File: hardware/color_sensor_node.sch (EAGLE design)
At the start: 20 parts, among them Q1 20V/4.2A/52mΩ/1.4W, U1 ISL29125, U2 3.3V, U3 WS2811

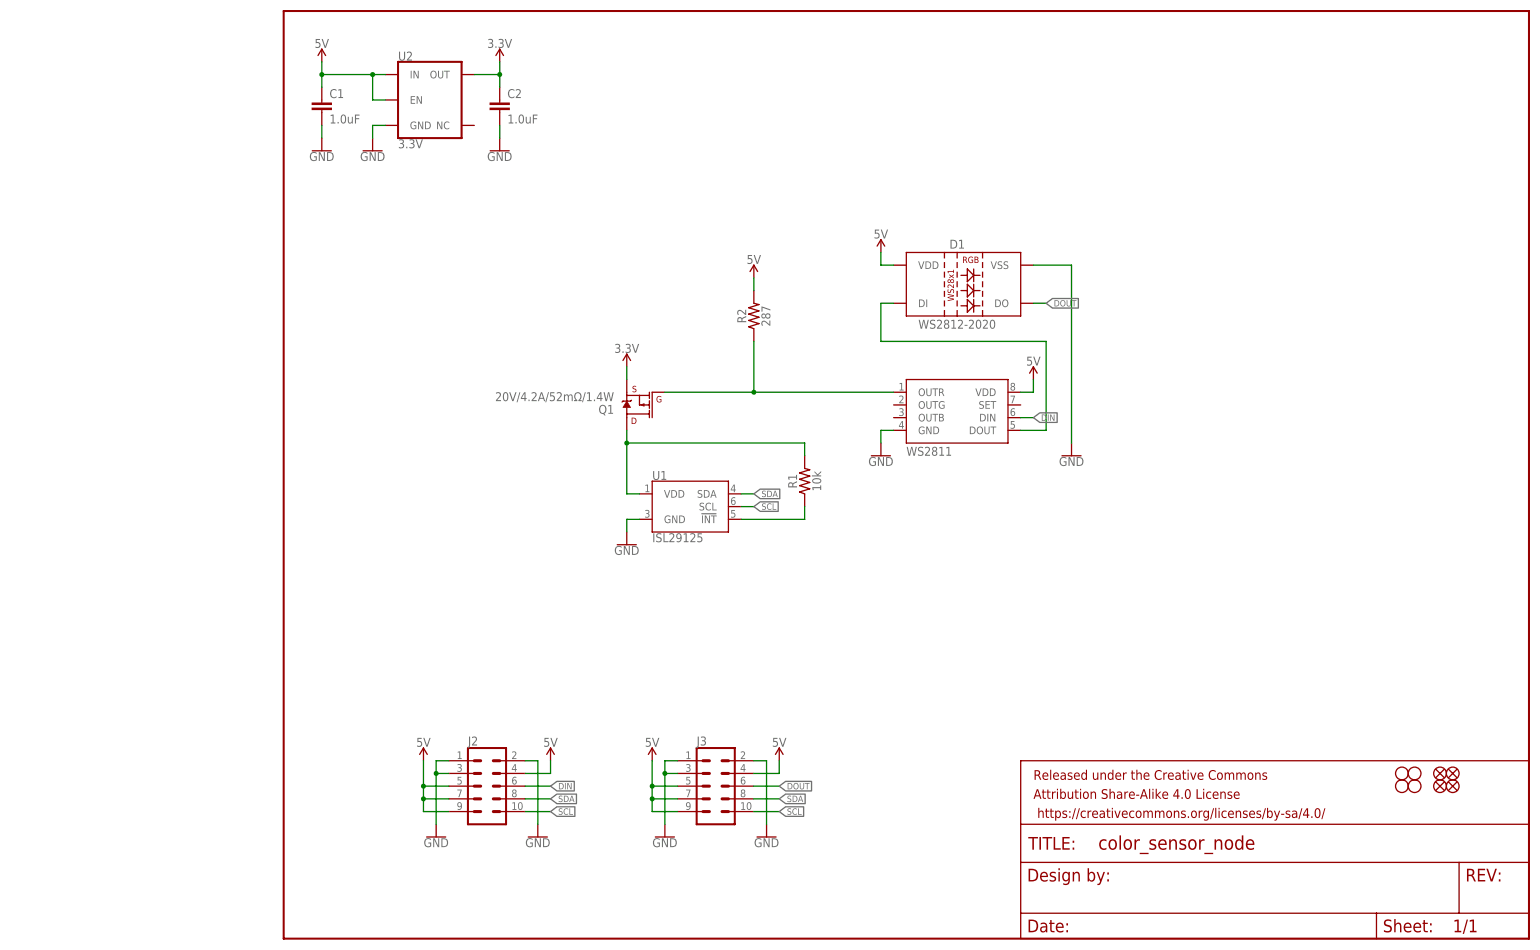
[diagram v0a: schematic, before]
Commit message: update packages, add rc filter to sensor vdd, move to smd connectors
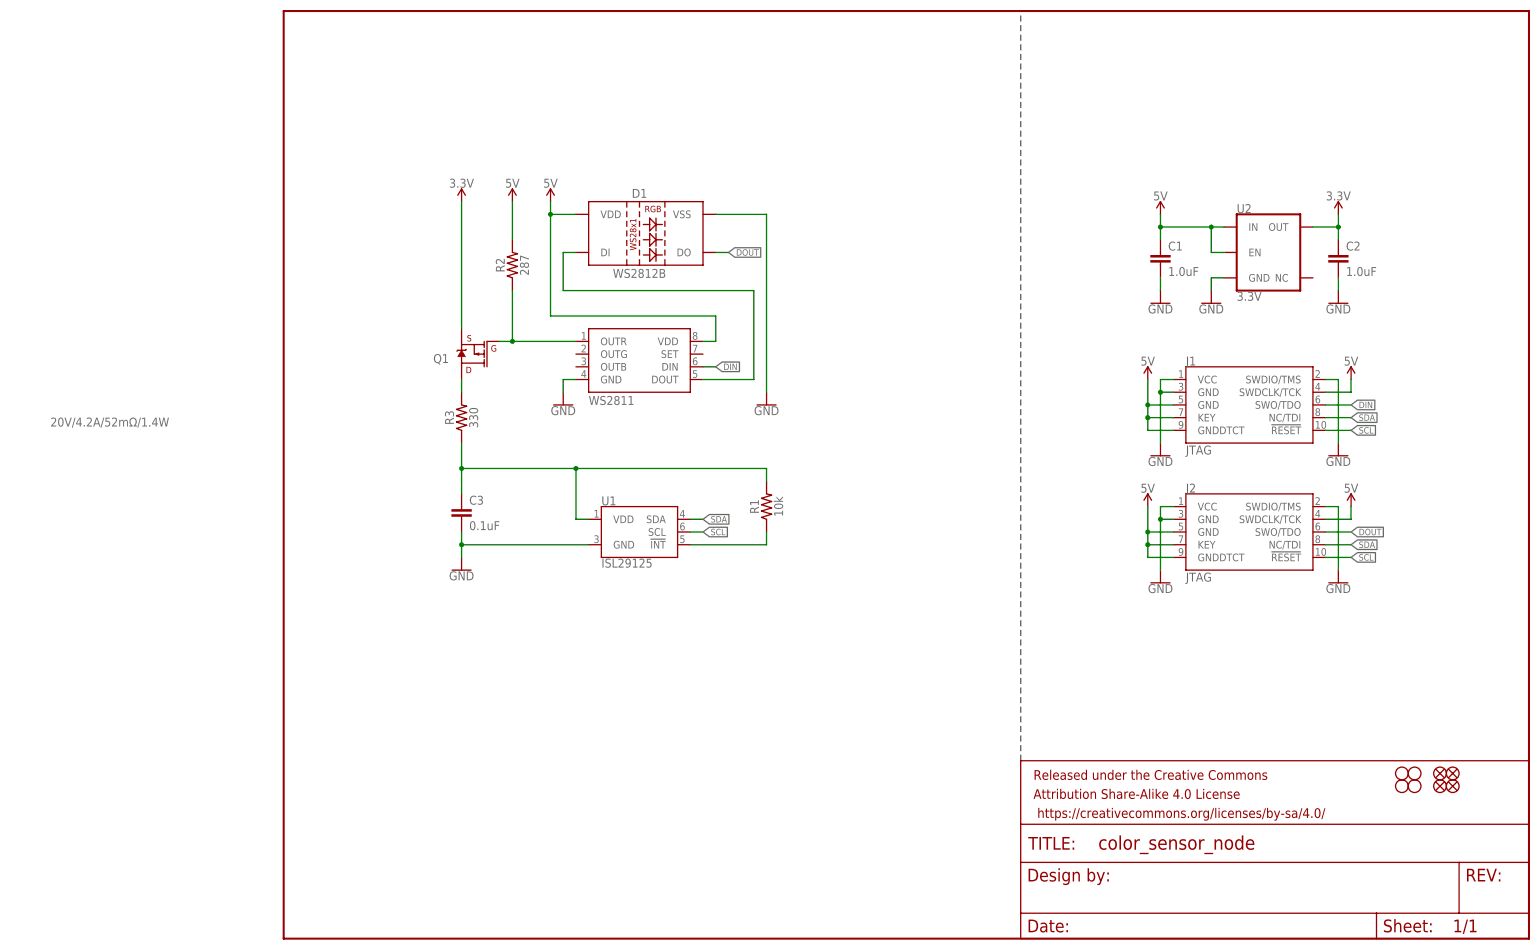
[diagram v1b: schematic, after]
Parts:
- removed J3: (no value), SparkFun-Connectors:CONN_05X20.05_IN_PTH_SILK
- added C3: 0.1uF, SparkFun-Capacitors:0.1UF-0603-25V-(+80/-20%)
- added J1: JTAG, SparkFun-Connectors:CORTEX_JTAG_DEBUG_SMD
- added R3: 330, SparkFun-Resistors:330OHM-0603-1/10W-1%
- D1: value WS2812-2020 -> WS2812B; device SparkFun-LED:WS2812-2020 -> SparkFun-LED:WS2812B
- J2: value (none) -> JTAG; device SparkFun-Connectors:CONN_05X20.05_IN_PTH_SILK -> SparkFun-Connectors:CORTEX_JTAG_DEBUG_SMD
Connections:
- new net N$5: Q1.D, R3.2
- net 5V: now also J1.GND@5, J1.GNDDTCT, J1.KEY, J1.SWDCLK/TCK, J2.GND@5, J2.GNDDTCT, J2.KEY, J2.SWDCLK/TCK; no longer J2.4, J2.5, J2.7, J2.9, J3.4, J3.5, J3.7, J3.9
- net DIN: now also J1.SWO/TDO; no longer J2.6
- net DOUT: now also J2.SWO/TDO; no longer J3.6
- net GND: now also C3.2, J1.GND@3, J1.SWDIO/TMS, J1.VCC, J2.GND@3, J2.SWDIO/TMS, J2.VCC; no longer J2.1, J2.2, J2.3, J3.1, J3.2, J3.3
- net N$2: now also C3.1, R3.1; no longer Q1.D
- net SCL: now also J1.!RESET, J2.!RESET; no longer J2.10, J3.10
- net SDA: now also J1.NC/TDI, J2.NC/TDI; no longer J2.8, J3.8
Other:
- moved on the sheet: C1, C2, D1, Q1, R1, R2, U1, U2

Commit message: simplify, remove mosfet
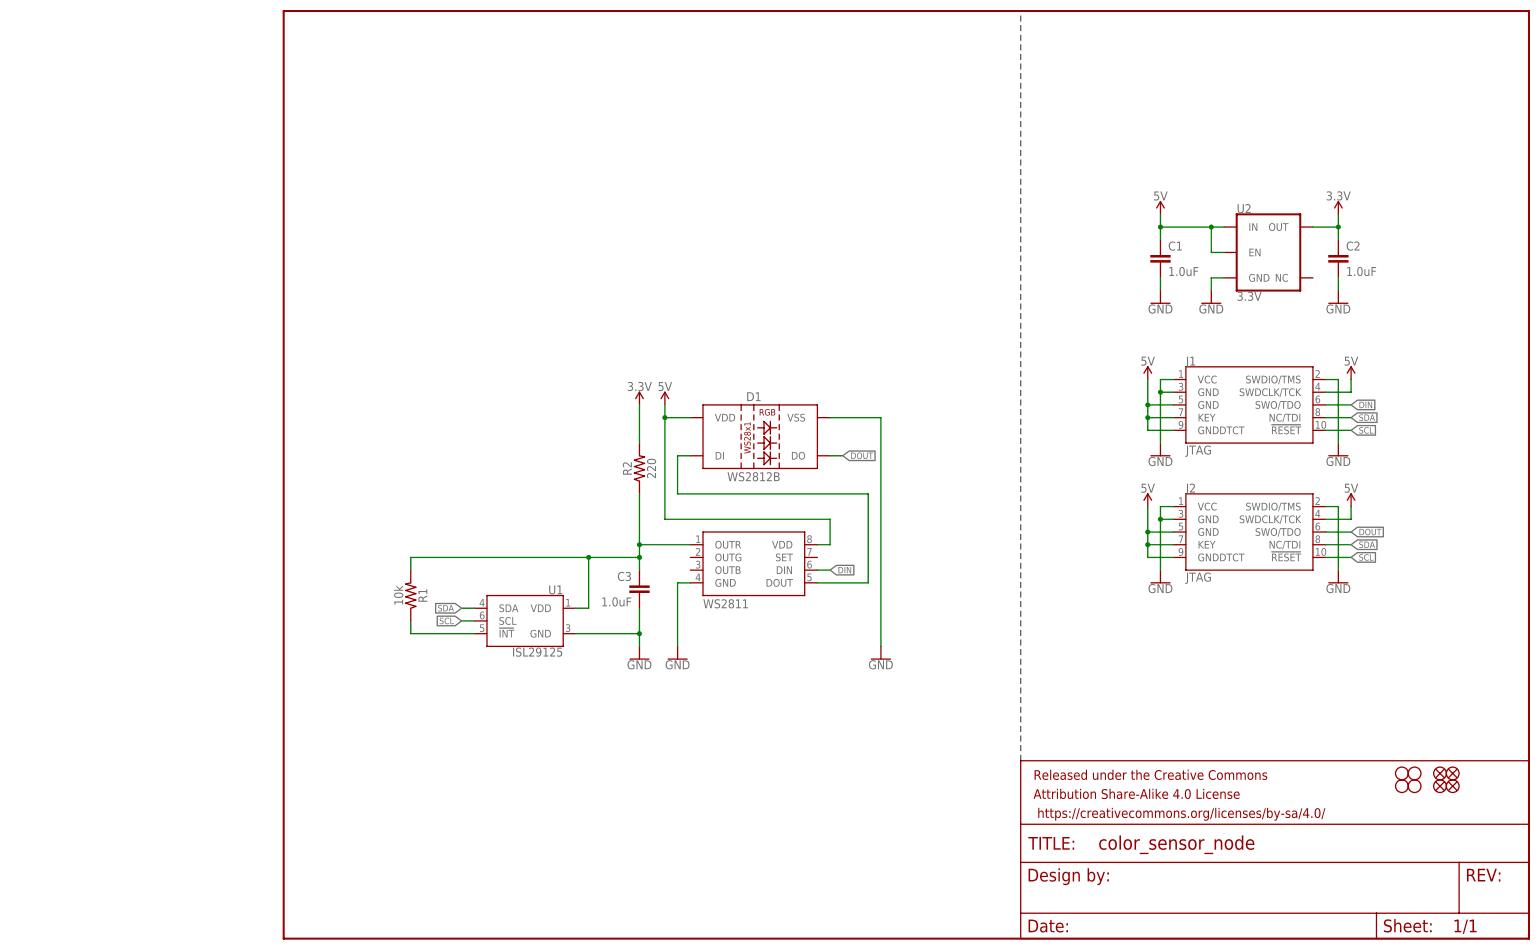
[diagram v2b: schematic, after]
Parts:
- removed Q1: 20V/4.2A/52mΩ/1.4W, SparkFun-DiscreteSemi:MOSFET_PCH-DMG2305UX-7
- removed R3: 330, SparkFun-Resistors:330OHM-0603-1/10W-1%
- C3: value 0.1uF -> 1.0uF; device SparkFun-Capacitors:0.1UF-0603-25V-(+80/-20%) -> SparkFun-Capacitors:1.0UF-0603-16V-10%
- R2: value 287 -> 220; device SparkFun-Resistors:287OHM-0603-1/10W-1% -> SparkFun-Resistors:220OHM-0603-1/10W-1%
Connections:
- removed net N$3: Q1.G, R2.1, U3.OUTR
- removed net N$5: Q1.D, R3.2
- net 3.3V: now also R2.2; no longer Q1.S
- net 5V: no longer R2.2
- net N$2: now also R2.1, U3.OUTR; no longer R3.1
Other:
- moved on the sheet: C3, D1, R1, R2, U1
